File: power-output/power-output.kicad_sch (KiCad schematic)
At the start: 11 parts, among them P1 USB_C_Plug_USB2.0, U1 AP2112K-3.3

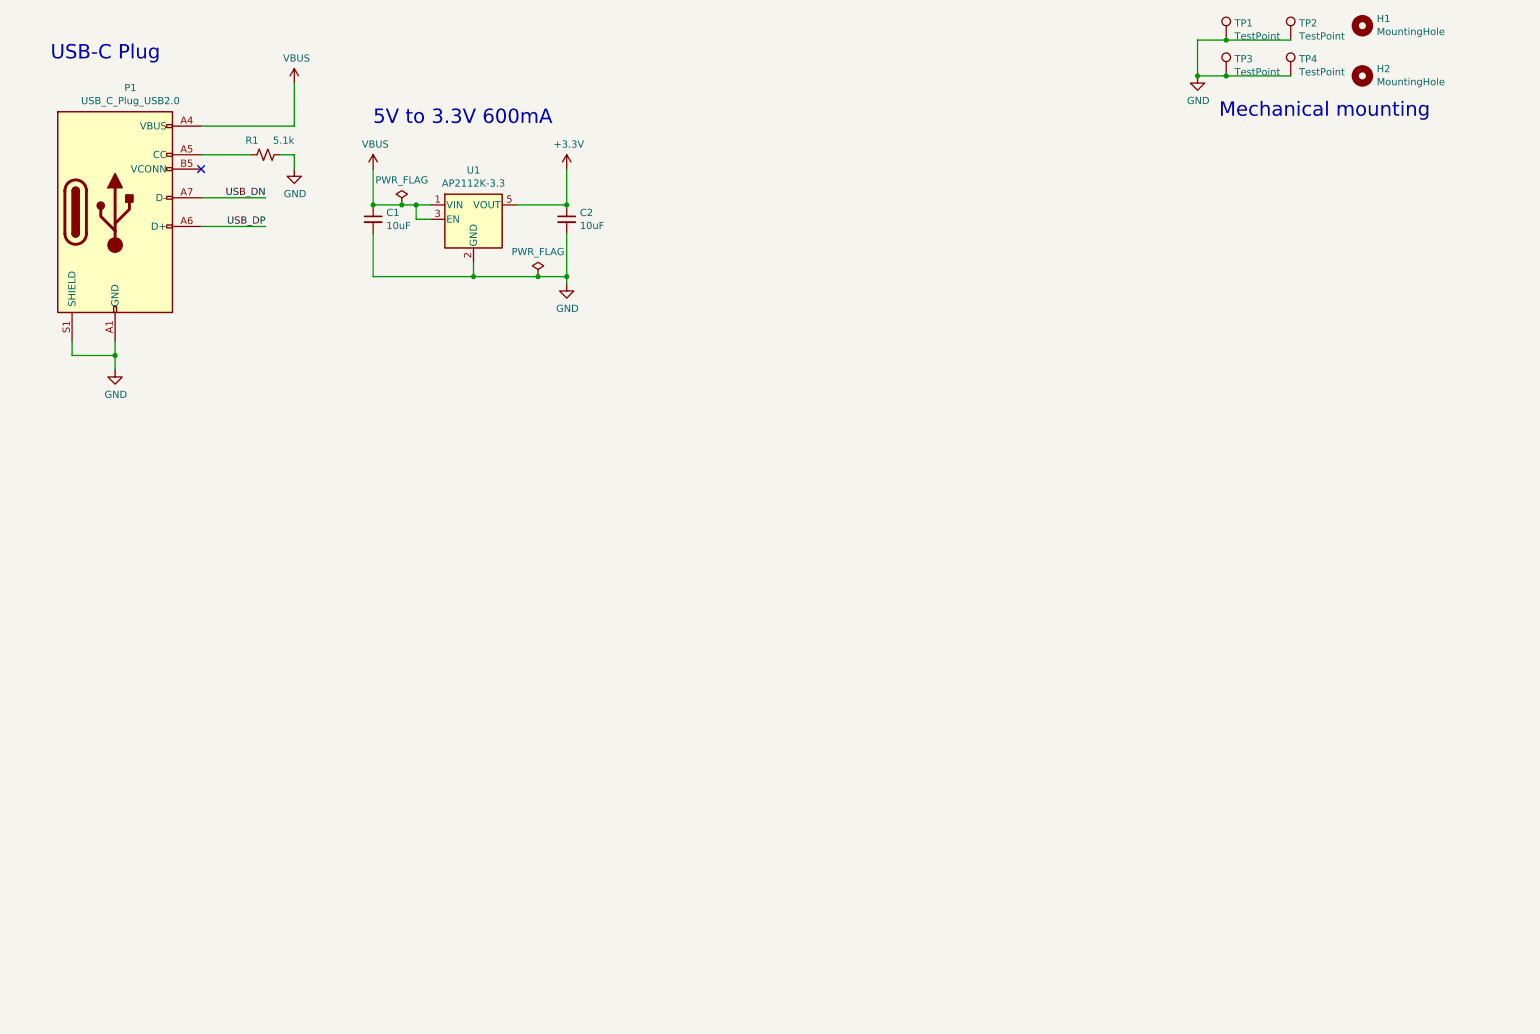
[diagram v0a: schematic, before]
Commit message: Added FUSB302BMPX
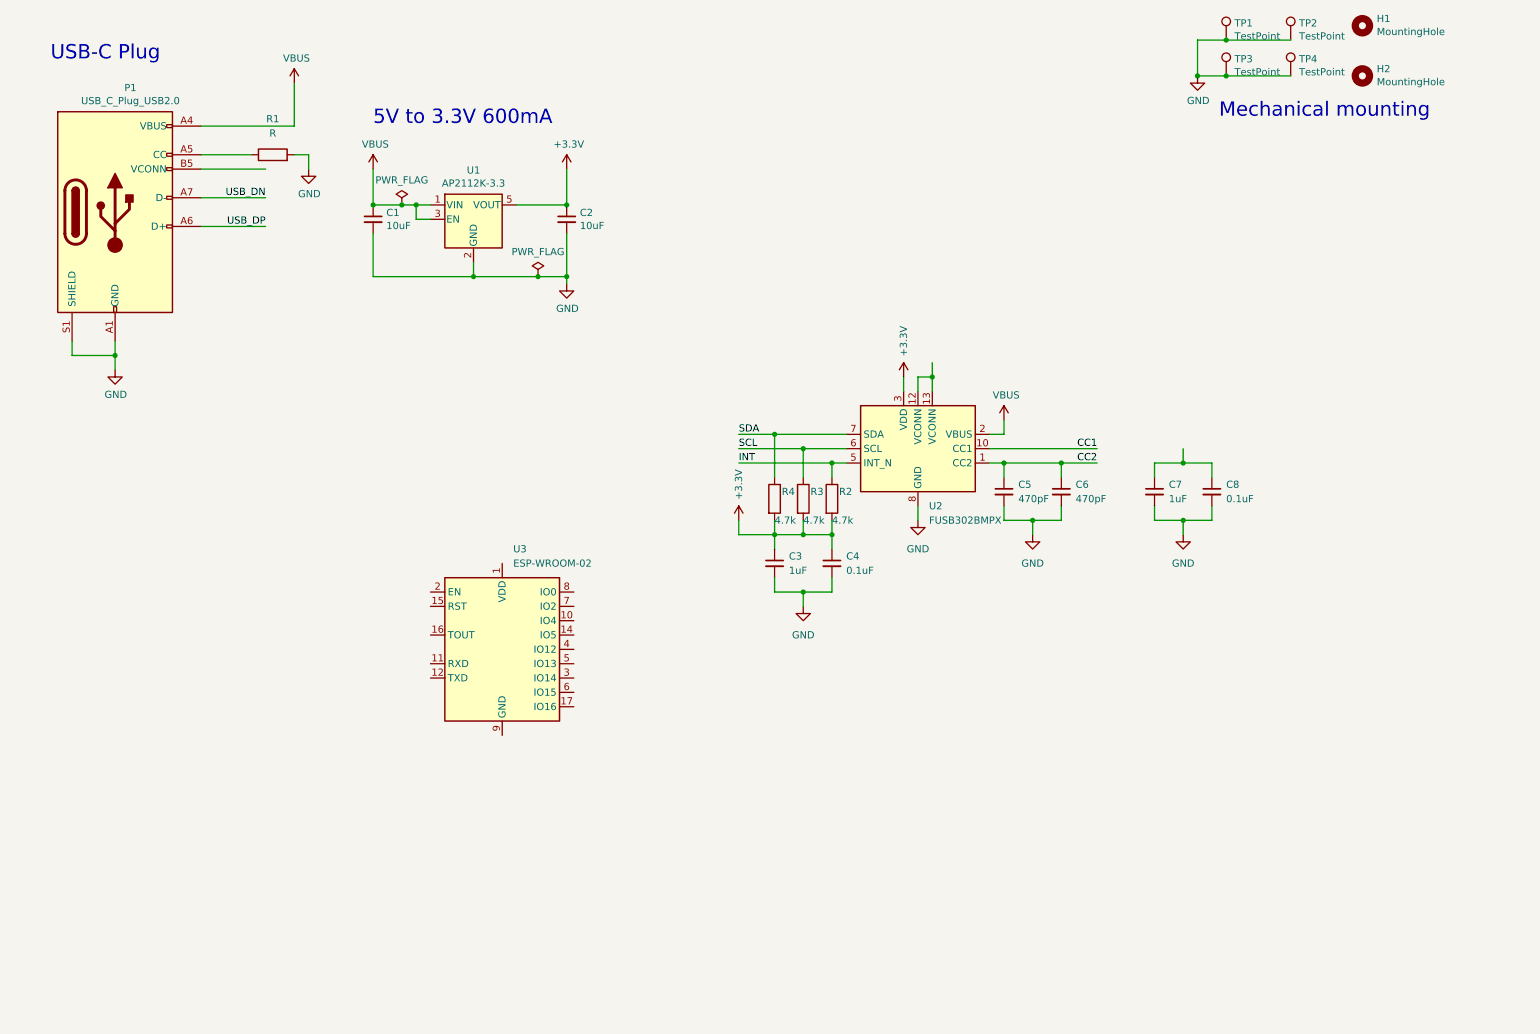
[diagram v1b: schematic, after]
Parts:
- removed R1: 5.1k, Resistor_SMD:R_0603_1608Metric, symbol Device:R_Small_US
- added C3, C7: 1uF, symbol Device:C_Small
- added C4, C8: 0.1uF, symbol Device:C_Small
- added C5, C6: 470pF, symbol Device:C_Small
- added R1: R, symbol Device:R
- added R2, R3, R4: 4.7k, symbol Device:R
- added U2: FUSB302BMPX, Package_DFN_QFN:WQFN-14-1EP_2.5x2.5mm_P0.5mm_EP1.45x1.45mm, symbol Interface_USB:FUSB302BMPX
- added U3: ESP-WROOM-02, RF_Module:ESP-WROOM-02, symbol RF_Module:ESP-WROOM-02
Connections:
- net +3.3V: now also C3.1, C4.1, R2.2, R3.2, R4.2, U2.3 (VDD), U2.4 (VDD)
- net GND: now also C3.2, C4.2, C5.2, C6.2, C7.2, C8.2, R1.2, U2.15 (GND), U2.8 (GND), U2.9 (GND)
- net VBUS: now also U2.2 (VBUS)
- net at P1.A5 (CC): now also R1.1
- new net: C7.1, C8.1
- new net: U3.13 (GND), U3.18 (GND), U3.19 (GND), U3.9 (GND)
- new net: U2.12 (VCONN), U2.13 (VCONN)
- new net CC1: U2.10 (CC1), U2.11 (CC1)
- new net CC2: C5.1, C6.1, U2.1 (CC2), U2.14 (CC2)
- new net INT: R2.1, U2.5 (INT_N)
- new net SCL: R3.1, U2.6 (SCL)
- new net SDA: R4.1, U2.7 (SDA)
- no-connect marks 1 -> 0

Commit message: Replaced ESP8266 with 8266EX
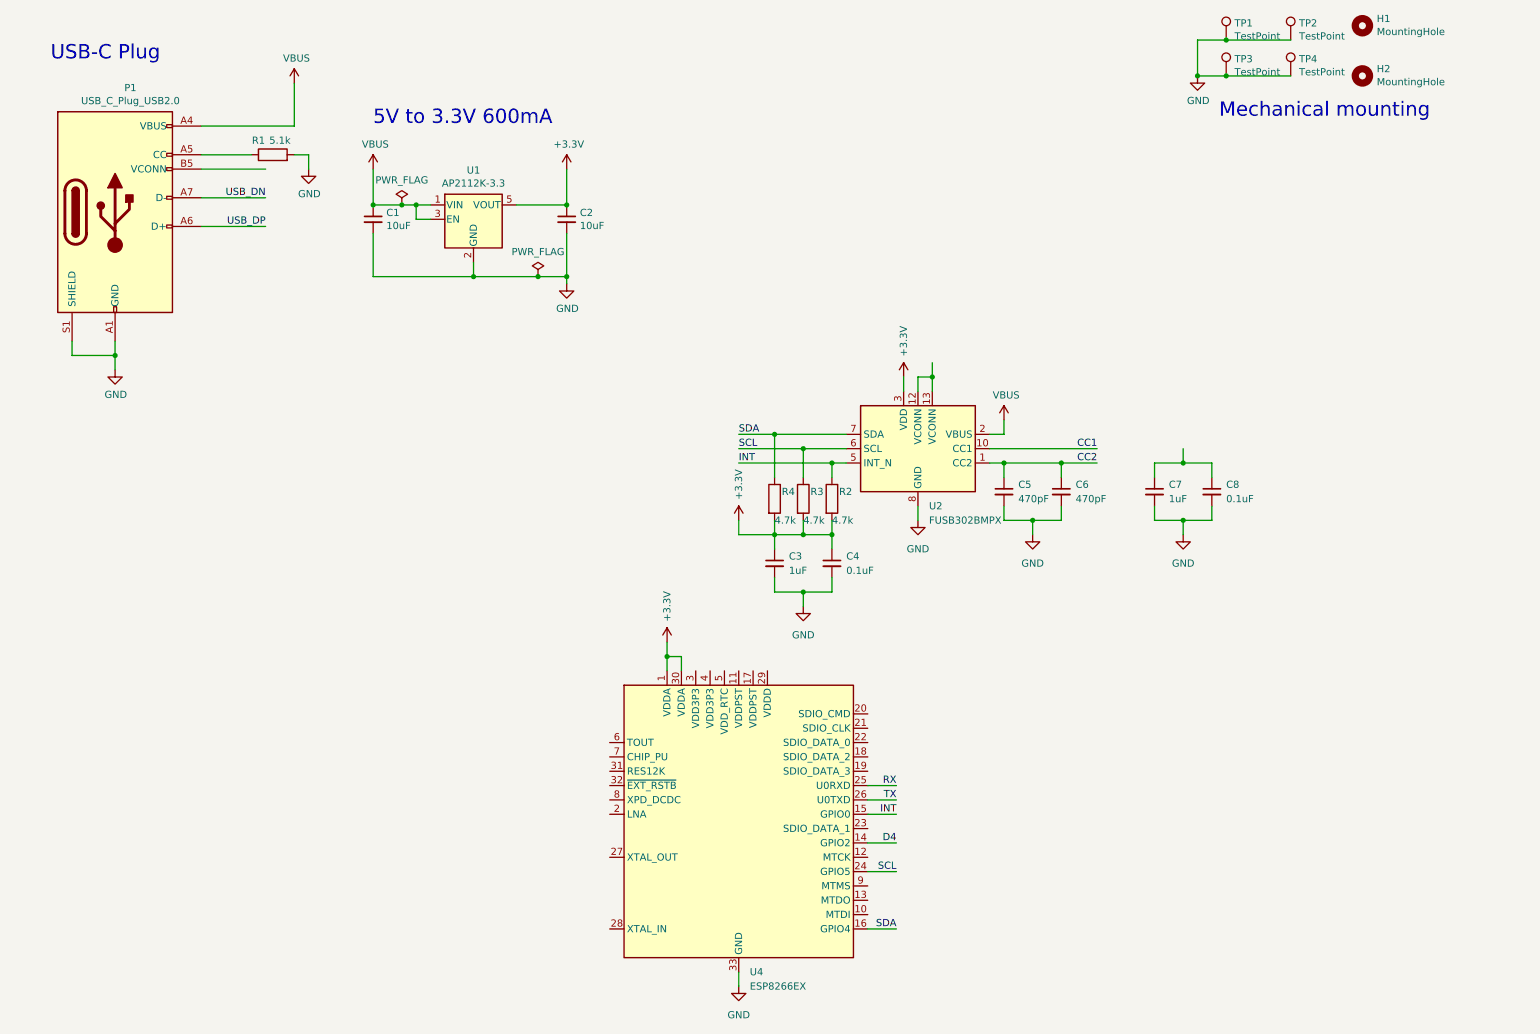
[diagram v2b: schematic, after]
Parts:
- removed U3: ESP-WROOM-02, RF_Module:ESP-WROOM-02, symbol RF_Module:ESP-WROOM-02
- added U4: ESP8266EX, Package_DFN_QFN:QFN-32-1EP_5x5mm_P0.5mm_EP3.45x3.45mm, symbol MCU_Espressif:ESP8266EX
- R1: value R -> 5.1k
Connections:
- net +3.3V: now also U4.1 (VDDA), U4.30 (VDDA)
- net GND: now also U4.33 (GND)
- net INT: now also U4.15 (GPIO0)
- net SCL: now also U4.24 (GPIO5)
- net SDA: now also U4.16 (GPIO4)
- new net D4: U4.14 (GPIO2)
- new net RX: U4.25 (U0RXD)
- new net TX: U4.26 (U0TXD)

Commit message: Added UART Interface
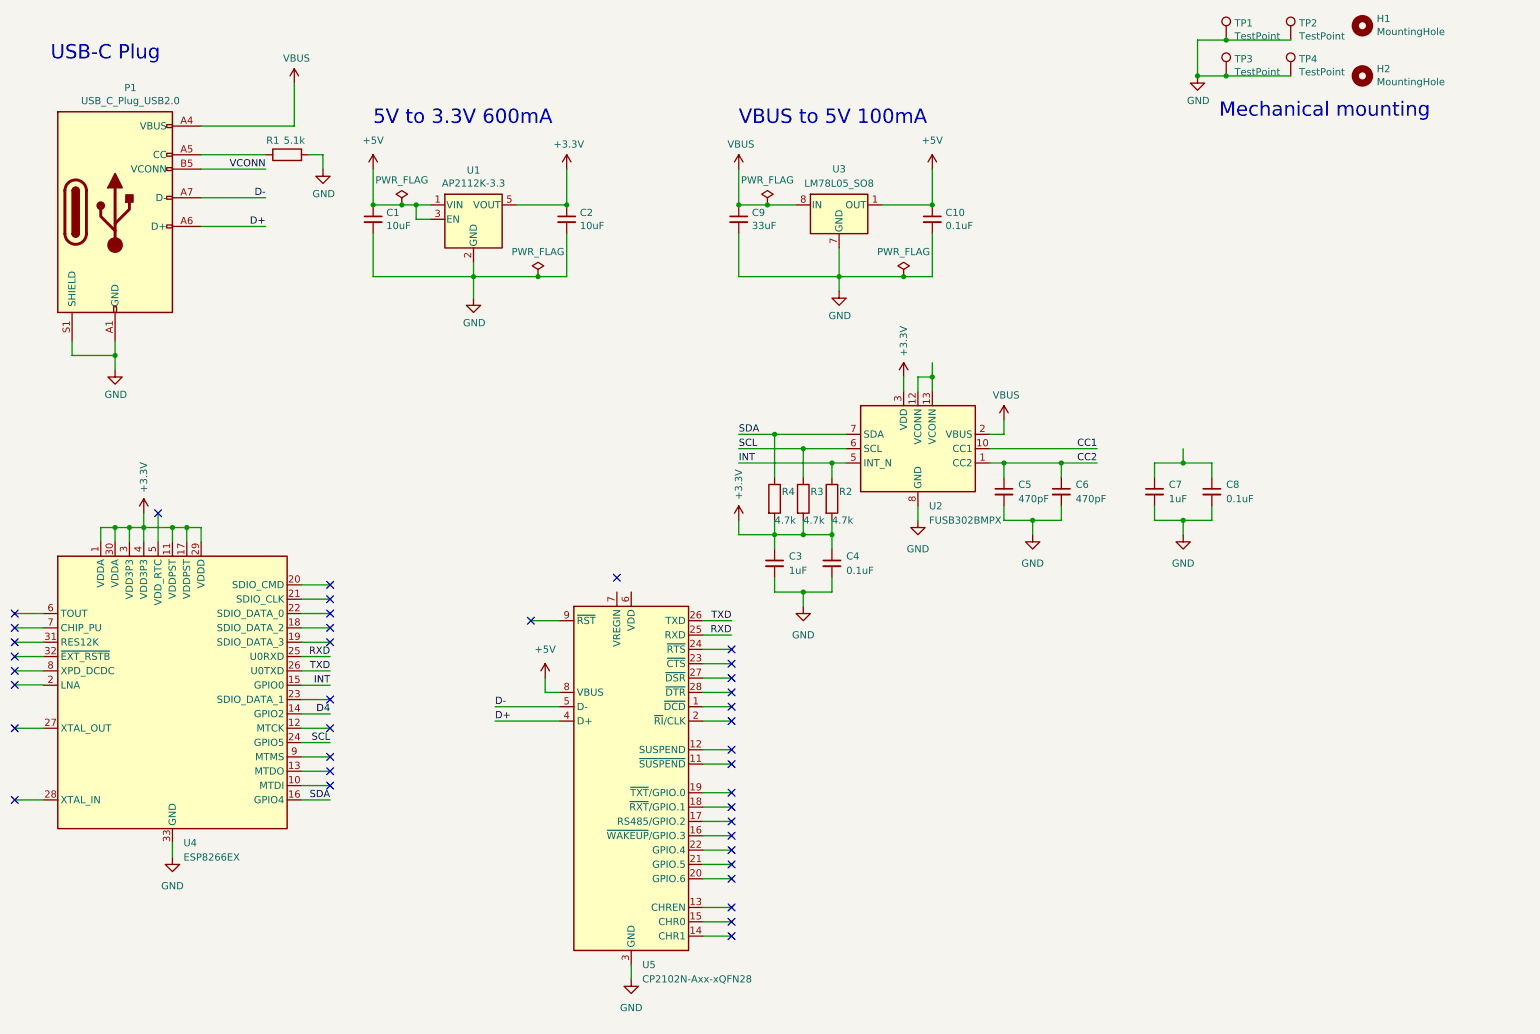
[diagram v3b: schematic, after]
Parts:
- added C10: 0.1uF, Capacitor_SMD:C_0201_0603Metric, symbol Device:C_Small
- added C9: 33uF, Capacitor_SMD:C_0201_0603Metric, symbol Device:C_Small
- added U3: LM78L05_SO8, Package_SO:SOIC-8_3.9x4.9mm_P1.27mm, symbol Regulator_Linear:LM78L05_SO8
- added U5: CP2102N-Axx-xQFN28, Package_DFN_QFN:QFN-28-1EP_5x5mm_P0.5mm_EP3.35x3.35mm, symbol Interface_USB:CP2102N-Axx-xQFN28
- C1, C2: footprint Capacitor_SMD:C_0805_2012Metric -> Capacitor_SMD:C_0201_0603Metric
- C3, C4, C5, C6, C7, C8: footprint (none) -> Capacitor_SMD:C_0201_0603Metric
- R1, R2, R3, R4: footprint (none) -> Resistor_SMD:R_0201_0603Metric
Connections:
- net +3.3V: now also U4.11 (VDDPST), U4.17 (VDDPST), U4.29 (VDDD), U4.3 (VDD3P3), U4.4 (VDD3P3)
- net GND: now also C10.2, C9.2, U3.2 (GND), U3.3 (GND), U3.6 (GND), U3.7 (GND), U5.29 (GND), U5.3 (GND)
- net VBUS: now also C9.1, U3.8 (IN); no longer C1.1, U1.1 (VIN), U1.3 (EN)
- net VCONN: now reaches P1.B5 (VCONN)
- net RX renamed RXD
- net RXD: now also U5.25 (RXD)
- net TX renamed TXD
- net TXD: now also U5.26 (TXD)
- net USB_DN renamed D-
- net D-: now also U5.5 (D-)
- net USB_DP renamed D+
- net D+: now also U5.4 (D+)
- new net +5V: C1.1, C10.1, U1.1 (VIN), U1.3 (EN), U3.1 (OUT), U5.8 (VBUS)
- no-connect marks 0 -> 39
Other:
- note added: "VBUS to 5V 100mA"
- moved on the sheet: R1, U4

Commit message: Cleaned up Schematics
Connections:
- net CC2 is gone; now on net CC1: C5.1, C6.1, U2.1 (CC2), U2.14 (CC2)
- net CC1: now also P1.A5 (CC), R1.1
- net VCONN: now also C7.1, C8.1, U2.12 (VCONN), U2.13 (VCONN)
- net D4: no longer names the net of U4.14 (GPIO2)
- no-connect marks 39 -> 40
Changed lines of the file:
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@@
   (junction (at 158.75 110.49) (diameter 0) (color 0 0 0 0)
   )
+  (junction (at 209.55 95.25) (diameter 0) (color 0 0 0 0)
+  )
   (junction (at 41.91 78.74) (diameter 0) (color 0 0 0 0)
   )
@@
   )
   (junction (at 181.61 64.77) (diameter 0) (color 0 0 0 0)
-  )
-  (junction (at 209.55 97.79) (diameter 0) (color 0 0 0 0)
   )
   (junction (at 52.07 109.22) (diameter 0) (color 0 0 0 0)
@@
   (no_connect (at 151.13 140.97))
   (no_connect (at 151.13 176.53))
+  (no_connect (at 80.01 142.24))
   (no_connect (at 80.01 152.4))
   (no_connect (at 24.13 132.08))
@@
   (no_connect (at 80.01 139.7))
   (no_connect (at 151.13 171.45))
-  (no_connect (at 24.13 137.0988))
+  (no_connect (at 24.13 137.16))
   (no_connect (at 151.13 148.59))
   (no_connect (at 151.13 135.89))
@@
     (stroke (width 0) (type default))
   )
-  (wire (pts (xy 209.55 97.79) (xy 209.55 100.33))
+  (wire (pts (xy 209.55 95.25) (xy 209.55 100.33))
     (stroke (width 0) (type default))
   )
@@
     (stroke (width 0) (type default))
   )
-  (wire (pts (xy 24.13 137.0988) (xy 29.21 137.0988))
+  (wire (pts (xy 24.13 137.16) (xy 29.21 137.16))
     (stroke (width 0) (type default))
   )
@@
     (stroke (width 0) (type default))
   )
+  (wire (pts (xy 209.55 95.25) (xy 215.9 95.25))
+    (stroke (width 0) (type default))
+  )
   (wire (pts (xy 158.75 120.65) (xy 163.83 120.65))
     (stroke (width 0) (type default))
@@
     (stroke (width 0) (type default))
   )
-  (wire (pts (xy 196.85 95.25) (xy 215.9 95.25))
+  (wire (pts (xy 196.85 95.25) (xy 209.55 95.25))
     (stroke (width 0) (type default))
   )
@@
     (stroke (width 0) (type default))
   )
-  (wire (pts (xy 199.39 97.79) (xy 209.55 97.79))
-    (stroke (width 0) (type default))
-  )
   (wire (pts (xy 121.92 45.72) (xy 121.92 52.07))
     (stroke (width 0) (type default))
@@
     (stroke (width 0) (type default))
   )
-  (wire (pts (xy 209.55 97.79) (xy 215.9 97.79))
+  (wire (pts (xy 199.39 97.79) (xy 215.9 97.79))
     (stroke (width 0) (type default))
   )
@@
     (effects (font (size 2.54 2.54)) (justify left bottom))
   )
-  (label "D4" (at 80.01 142.24 180) (fields_autoplaced)
-    (effects (font (size 1.27 1.27)) (justify right bottom))
-  )
   (label "RXD" (at 80.01 132.08 180) (fields_autoplaced)
     (effects (font (size 1.27 1.27)) (justify right bottom))
@@
   (label "D-" (at 68.58 50.8 180) (fields_autoplaced)
     (effects (font (size 1.27 1.27)) (justify right bottom))
+  )
+  (label "VCONN" (at 186.69 80.01 90) (fields_autoplaced)
+    (effects (font (size 1.27 1.27)) (justify left bottom))
   )
   (label "D+" (at 68.58 55.88 180) (fields_autoplaced)
@@
     (effects (font (size 1.27 1.27)) (justify left bottom))
   )
+  (label "CC1" (at 60.96 43.18 180) (fields_autoplaced)
+    (effects (font (size 1.27 1.27)) (justify right bottom))
+  )
   (label "CC2" (at 215.9 97.79 180) (fields_autoplaced)
     (effects (font (size 1.27 1.27)) (justify right bottom))
@@
   (label "INT" (at 80.01 137.16 180) (fields_autoplaced)
     (effects (font (size 1.27 1.27)) (justify right bottom))
+  )
+  (label "VCONN" (at 231.14 95.25 90) (fields_autoplaced)
+    (effects (font (size 1.27 1.27)) (justify left bottom))
   )
   (label "SDA" (at 152.4 92.71 0) (fields_autoplaced)
@@
     (effects (font (size 1.27 1.27)) (justify left bottom))
   )
+  (label "CC2" (at 66.04 43.18 180) (fields_autoplaced)
+    (effects (font (size 1.27 1.27)) (justify right bottom))
+  )
   (label "INT" (at 152.4 97.79 0) (fields_autoplaced)
